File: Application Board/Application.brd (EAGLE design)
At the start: 101.6 x 101.6 mm, 57 parts, among them Q1 DMP2012SN-7, T1 FDN340P, T2 AP1117_LIN_REG, U1 LM3409HV'LM3409HV'

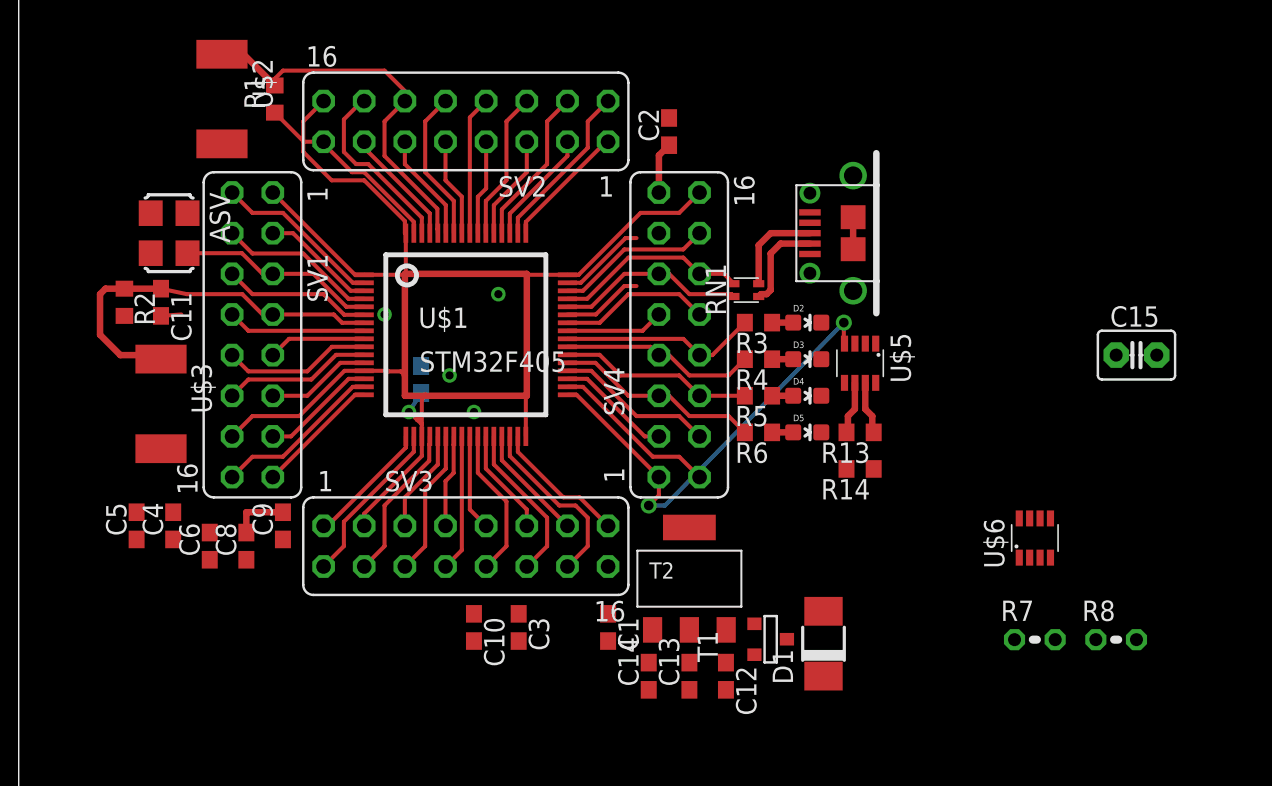
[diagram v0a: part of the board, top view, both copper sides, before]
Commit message: Moved capacitors around
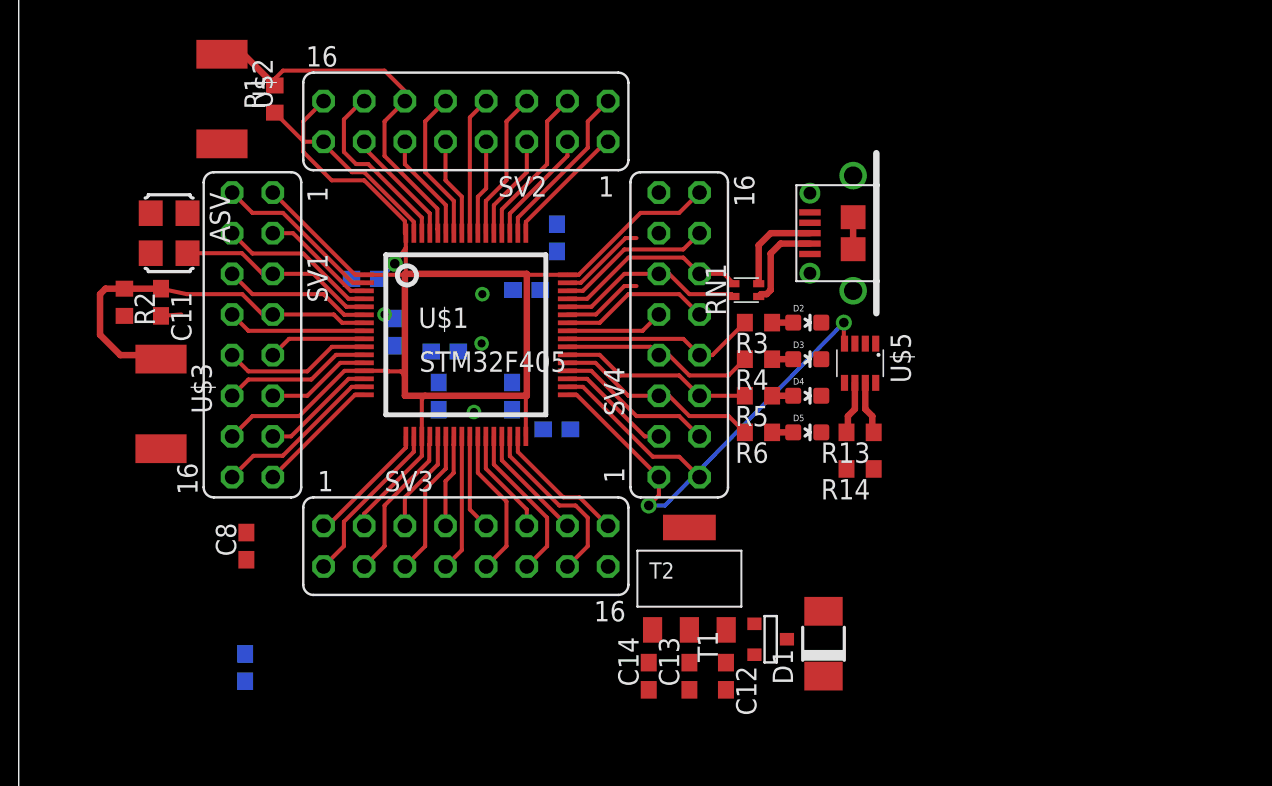
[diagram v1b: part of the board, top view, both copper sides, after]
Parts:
- removed C15: 1 uF, capacitor-wima:C2.5-3
- removed R7: 120, resistor:0204V
- removed R8: 100k, resistor:0204V
- removed U$6: MAX3051MAX3051, MAX3051 Library:SOT23-8L
- moved C5 31.8 mm to (33.6, 41.6), flipped to the bottom
- moved C4 24.7 mm to (33.6, 29.7), flipped to the bottom, turned to 180 degrees
- moved C7 21.1 mm to (14.1, 14.8)
- moved C6 19.3 mm to (21.6, 39.1), flipped to the bottom, turned to 0 degrees
- moved C10 19.1 mm to (23.4, 35.7), flipped to the bottom, turned to 90 degrees
- moved C1 15.7 mm to (30.8, 31.7), flipped to the bottom, turned to 90 degrees
- moved C3 15.3 mm to (26.2, 31.7), flipped to the bottom, turned to 90 degrees
- moved C9 14.9 mm to (26.6, 34.5), flipped to the bottom, turned to 180 degrees
- moved C2 13.3 mm to (31.7, 38.4), flipped to the bottom, turned to 0 degrees
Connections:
- removed net CANH1: R7.1, U$6.7
- removed net CANL1: R7.2, U$6.6
- removed net N$19: R8.1, U$6.8
- removed net RXD: U$6.4
- removed net TXD: U$6.1
- removed net VCC: C15.2, U$6.3
- net GND: no longer C15.1, R8.2, U$6.2
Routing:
- net GND: track 62.0 -> 58.5 mm
- net VCAP_2: track 3.22 -> 0.00 mm

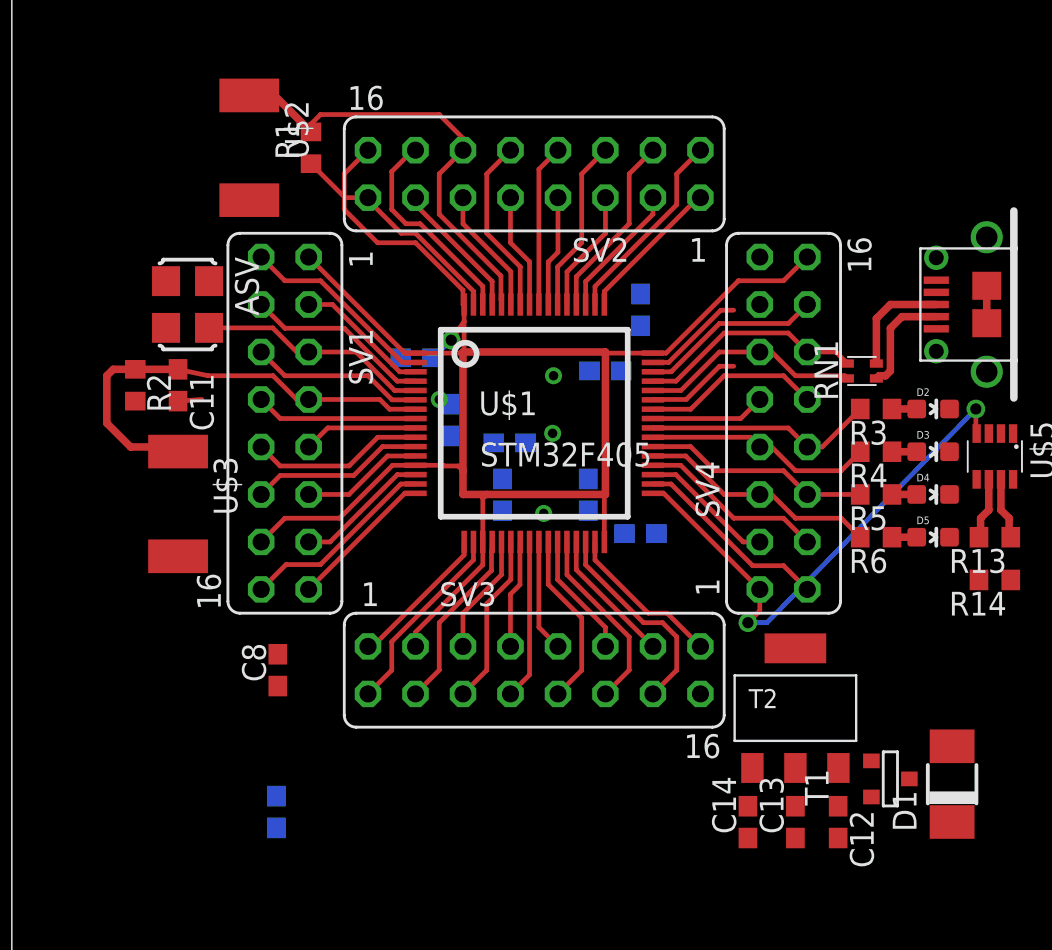
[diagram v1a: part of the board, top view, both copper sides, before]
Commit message: Fixed all the routing on the microcontroller.
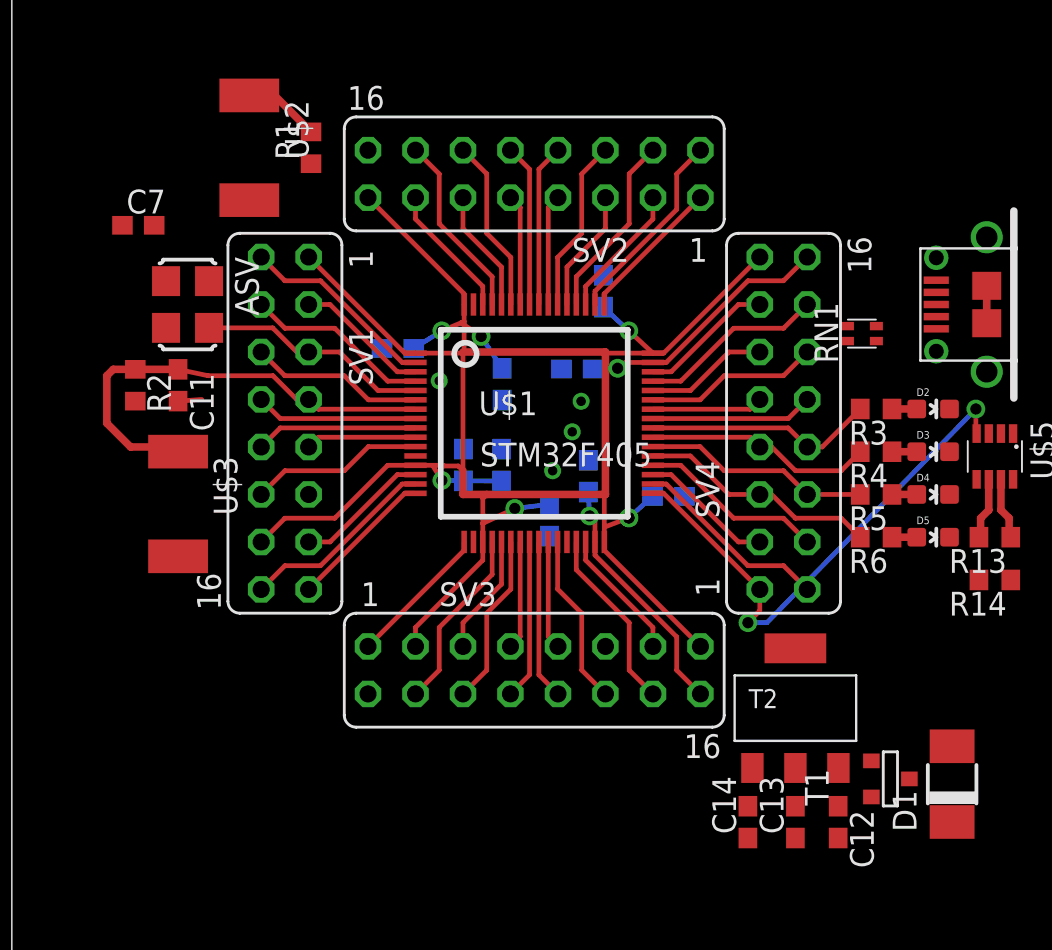
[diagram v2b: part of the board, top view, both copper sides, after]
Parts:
- moved C7 32.2 mm to (6.77, 46.1), flipped to the top, turned to 0 degrees
- moved C8 19.4 mm to (26.2, 37.6), flipped to the bottom, turned to 270 degrees
- moved C3 2.86 mm to (28.8, 30.4), turned to 270 degrees
- moved C4 2.50 mm to (35.1, 31.7)
- moved C10 2.50 mm to (24.1, 33.3)
- moved C5 2.24 mm to (31.6, 42.6)
- moved RN1 2.00 mm to (45.5, 40.4)
- moved C2 1.50 mm to (30.2, 38.5)
- moved C9 1.26 mm to (26.2, 33.3), turned to 90 degrees
- moved C6 1.12 mm to (20.6, 39.6)
- moved C1 1.00 mm to (30.8, 32.7)
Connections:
- removed net PIN45: SV4.13
- net +3V3: now also SV2.15, SV3.15, SV4.15; no longer SV2.16, SV3.16, SV4.16
- net BOOT0: now also SV2.11; no longer SV2.12
- net GND: now also SV2.16, SV3.11; no longer SV2.15, SV3.12
- net PIN25: now also SV3.10; no longer SV3.9
- net PIN26: now also SV3.9; no longer SV3.10
- net PIN27: now also SV3.12; no longer SV3.11
- net PIN29: now also SV3.14; no longer SV3.13
- net PIN30: now also SV3.13; no longer SV3.14
- net PIN41: now also SV4.10; no longer SV4.9
- net PIN42: now also SV4.9; no longer SV4.10
- net PIN43: now also SV4.12
- net PIN46: now also SV4.13; no longer SV4.14
- net PIN57: now also SV2.10; no longer SV2.9
- net PIN59: now also SV2.12; no longer SV2.11
- net PIN61: now also SV2.14; no longer SV2.13
- net PIN62: now also SV2.13; no longer SV2.14
- net SHFT_REG_CLK: now also SV1.10; no longer SV1.9
- net SHFT_REG_EN: now also SV1.9; no longer SV1.10
- net TEMP_SENS: now also SV2.9; no longer SV2.10
- net USBD+: now also SV4.14; no longer SV4.12
- net VCAP_1: now also SV3.16; no longer SV3.15
- net VCAP_2: now also SV4.16; no longer SV4.15
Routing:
- net GND: track 58.5 -> 19.1 mm
- net +3V3: track 96.5 -> 115.3 mm, vias 1 -> 7
- net VCAP_2: track 0.00 -> 13.9 mm, vias 0 -> 1
- net BOOT0: track 24.5 -> 11.0 mm
- net PIN43: track 0.00 -> 9.32 mm
- net N$24: track 5.92 -> 0.00 mm
- net N$1: track 5.91 -> 0.00 mm
- net USBD-: track 11.8 -> 6.57 mm
- net N$3: track 5.25 -> 0.00 mm
- net N$2: track 5.05 -> 0.00 mm
- net VCAP_1: track 8.52 -> 13.3 mm, vias 0 -> 1
- net PIN30: track 11.3 -> 7.08 mm
- net PIN62: track 11.3 -> 7.21 mm
- net TEMP_SENS: track 9.52 -> 5.93 mm
- net PIN42: track 9.52 -> 5.93 mm
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
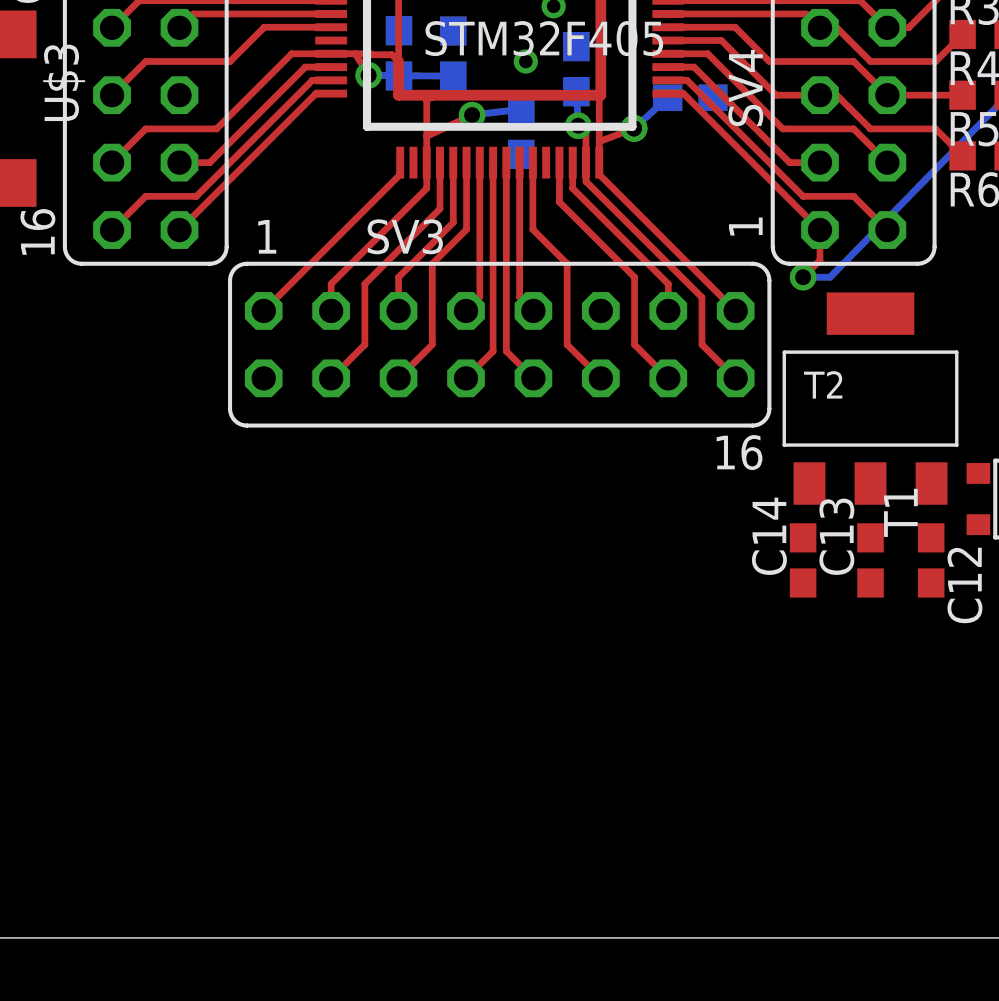
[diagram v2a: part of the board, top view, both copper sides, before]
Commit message: added order of board input voltage and signals
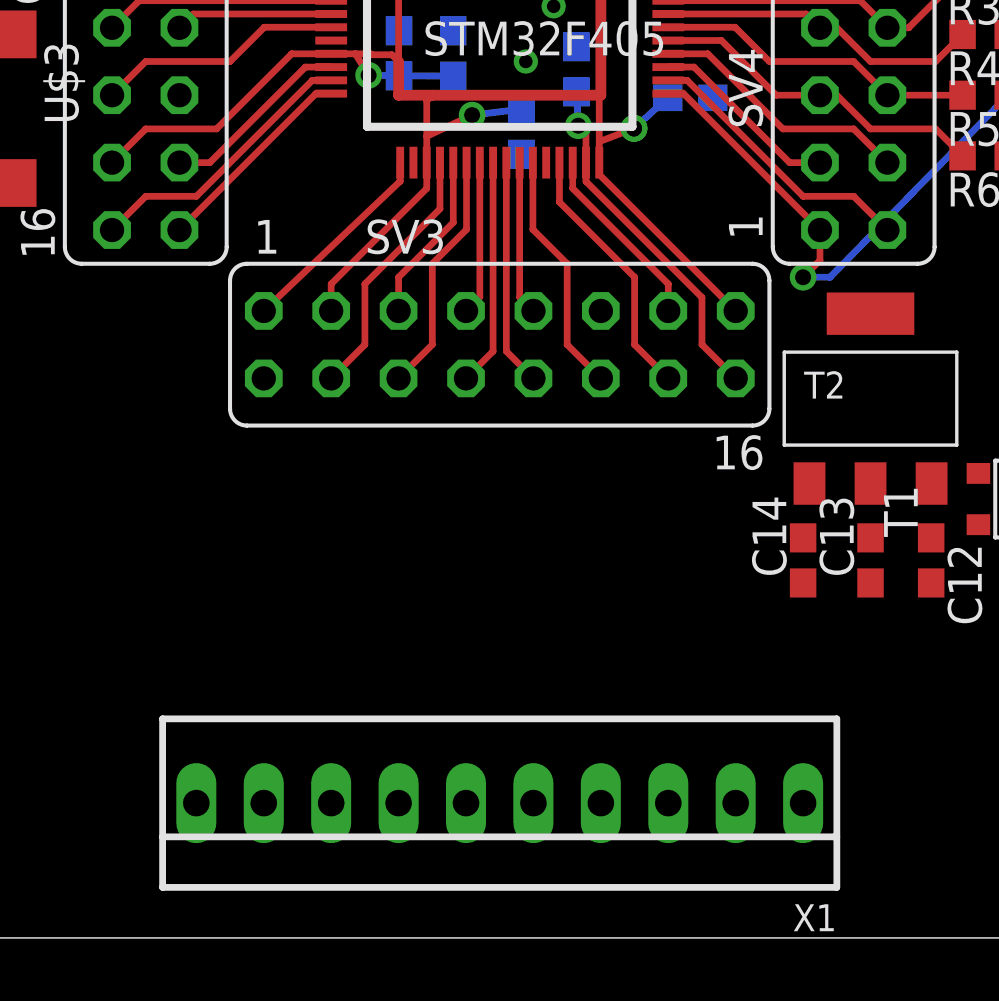
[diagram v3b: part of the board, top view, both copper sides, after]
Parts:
- added X1: 22-23-2101, con-molex:22-23-2101
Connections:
- new net 12V: X1.10
- net +5V: now also X1.9
- net CAM_LED: now also X1.1
- net CANH: now also X1.7
- net CANL: now also X1.6
- net GND: now also X1.8
- net SHFT_REG_CLK: now also X1.3
- net SHFT_REG_DATA: now also X1.4
- net SHFT_REG_EN: now also X1.2
- net TEMP_SENS: now also X1.5
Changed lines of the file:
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@@
 <attribute name="VALUE" x="34.417" y="76.2" size="1.27" layer="27" rot="R180"/>
+</element>
+<element name="X1" library="con-molex" package="22-23-2101" value="22-23-2101" x="27.94" y="5.08" rot="R180">
+<attribute name="MF" value="MOLEX" x="27.94" y="5.08" size="1.778" layer="27" rot="R180" display="off"/>
+<attribute name="OC_FARNELL" value="1756828" x="27.94" y="5.08" size="1.778" layer="27" rot="R180" display="off"/>
+<attribute name="OC_NEWARK" value="94C0765" x="27.94" y="5.08" size="1.778" layer="27" rot="R180" display="off"/>
+<attribute name="MPN" value="22-23-2101" x="27.94" y="5.08" size="1.778" layer="27" rot="R180" display="off"/>
 </element>
 </elements>
@@
 <contactref element="T2" pad="GND"/>
 <contactref element="SV1" pad="11"/>
-<wire x1="18.034" y1="31.75" x2="15.875" y2="31.75" width="0" layer="19" extent="1-16"/>
-<wire x1="21.59" y1="33.81" x2="20.094" y2="33.81" width="0" layer="19" extent="1-16"/>
-<wire x1="20.094" y1="33.81" x2="18.034" y2="31.75" width="0" layer="19" extent="1-16"/>
-<wire x1="24.69" y1="41.91" x2="24.69" y2="42.62" width="0" layer="19" extent="1-16"/>
 <wire x1="50.038" y1="29.349" x2="50.153" y2="29.464" width="0.4064" layer="1"/>
 <wire x1="8.89" y1="36.742" x2="10.16" y2="36.83" width="0.254" layer="1"/>
@@
 <contactref element="SV3" pad="11"/>
 <contactref element="SV2" pad="16"/>
+<contactref element="X1" pad="8"/>
 <wire x1="33.821" y1="73.191" x2="33.528" y2="73.914" width="0" layer="19" extent="1-16"/>
 <wire x1="31.877" y1="71.755" x2="32.258" y2="71.628" width="0" layer="19" extent="1-1"/>
@@
 <wire x1="8.89" y1="36.742" x2="8.248" y2="40.66" width="0" layer="19" extent="1-1"/>
 <wire x1="15.875" y1="31.75" x2="10.16" y2="36.83" width="0" layer="19" extent="1-1"/>
+<wire x1="21.59" y1="33.81" x2="15.875" y2="31.75" width="0" layer="19" extent="1-1"/>
 <wire x1="24.148" y1="34.178" x2="21.59" y2="33.81" width="0" layer="19" extent="1-16"/>
 <wire x1="26.19" y1="34.172" x2="24.148" y2="34.178" width="0" layer="19" extent="16-16"/>
@@
 <wire x1="49.444" y1="39.41" x2="52.144" y2="38.3125" width="0" layer="19" extent="1-1"/>
 <wire x1="52.903" y1="35.007" x2="50.153" y2="34.036" width="0" layer="19" extent="1-1"/>
+<wire x1="21.59" y1="5.08" x2="19.05" y2="21.082" width="0" layer="19" extent="1-1"/>
 </signal>
 <signal name="OSCIN">
@@
 <contactref element="U$1" pad="17"/>
 <contactref element="SV3" pad="1"/>
-<wire x1="24.19" y1="29.21" x2="24.19" y2="28.762" width="0.254" layer="1"/>
-<wire x1="24.19" y1="28.762" x2="19.05" y2="23.622" width="0.254" layer="1"/>
+<wire x1="24.19" y1="29.21" x2="24.19" y2="28.508" width="0.254" layer="1"/>
+<wire x1="24.19" y1="28.508" x2="19.05" y2="23.622" width="0.254" layer="1"/>
 </signal>
 <signal name="PIN20">
@@
 <contactref element="T1" pad="3"/>
 <contactref element="D1" pad="A"/>
+<contactref element="X1" pad="9"/>
 <wire x1="45.974" y1="17.5006" x2="50.292" y2="18.281" width="0" layer="19" extent="1-1"/>
+<wire x1="19.05" y1="5.08" x2="45.974" y2="17.5006" width="0" layer="19" extent="1-1"/>
 </signal>
 <signal name="N$58">
@@
 <wire x1="51.816" y1="30.48" x2="51.816" y2="29.552" width="0.4064" layer="1"/>
 <wire x1="51.816" y1="29.552" x2="51.728" y2="29.464" width="0.4064" layer="1"/>
+<contactref element="X1" pad="6"/>
+<wire x1="26.67" y1="5.08" x2="51.728" y2="29.464" width="0" layer="19" extent="1-1"/>
 </signal>
 <signal name="CANH">
@@
 <wire x1="53.34" y1="30.48" x2="53.34" y2="29.552" width="0.4064" layer="1"/>
 <wire x1="53.34" y1="29.552" x2="53.428" y2="29.464" width="0.4064" layer="1"/>
+<contactref element="X1" pad="7"/>
+<wire x1="24.13" y1="5.08" x2="53.34" y2="29.552" width="0" layer="19" extent="1-1"/>
 </signal>
 <signal name="N$63">
@@
 <wire x1="21.59" y1="35.81" x2="14.355" y2="35.81" width="0.254" layer="1"/>
 <wire x1="14.355" y1="35.81" x2="13.335" y2="36.83" width="0.254" layer="1"/>
+<contactref element="X1" pad="4"/>
+<wire x1="31.75" y1="5.08" x2="14.355" y2="35.81" width="0" layer="19" extent="1-1"/>
 </signal>
 <signal name="SHFT_REG_CLK">
@@
 <wire x1="21.59" y1="35.31" x2="14.355" y2="35.31" width="0.254" layer="1"/>
 <wire x1="14.355" y1="35.31" x2="13.335" y2="34.29" width="0.254" layer="1"/>
+<contactref element="X1" pad="3"/>
+<wire x1="34.29" y1="5.08" x2="13.335" y2="34.29" width="0" layer="19" extent="1-1"/>
 </signal>
 <signal name="SHFT_REG_EN">
@@
 <wire x1="21.59" y1="34.81" x2="16.395" y2="34.81" width="0.254" layer="1"/>
 <wire x1="16.395" y1="34.81" x2="15.875" y2="34.29" width="0.254" layer="1"/>
+<contactref element="X1" pad="2"/>
+<wire x1="36.83" y1="5.08" x2="15.875" y2="34.29" width="0" layer="19" extent="1-1"/>
 </signal>
 <signal name="CAM_LED">
@@
 <wire x1="25.4" y1="25.4" x2="25.4" y2="22.352" width="0.254" layer="1"/>
 <wire x1="25.4" y1="22.352" x2="24.13" y2="21.082" width="0.254" layer="1"/>
+<contactref element="X1" pad="1"/>
+<wire x1="39.37" y1="5.08" x2="24.13" y2="21.082" width="0" layer="19" extent="1-1"/>
 </signal>
 <signal name="CAN2_RX">
@@
 <wire x1="27.19" y1="41.91" x2="27.19" y2="47.105" width="0.254" layer="1"/>
 <wire x1="27.19" y1="47.105" x2="26.67" y2="47.625" width="0.254" layer="1"/>
+<contactref element="X1" pad="5"/>
+<wire x1="29.21" y1="5.08" x2="27.19" y2="41.91" width="0" layer="19" extent="1-1"/>
 </signal>
 <signal name="N$2">
@@
 <wire x1="29.337" y1="75.565" x2="29.337" y2="78.867" width="0.3048" layer="1"/>
 </signal>
+<signal name="12V">
+<contactref element="X1" pad="10"/>
+</signal>
 </signals>
